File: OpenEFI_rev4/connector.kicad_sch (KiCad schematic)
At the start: 23 parts, among them J6 1241434-1, Q10 IRF540N, Q5 SS8050, Q6 IRLZ44N, Q7 IRLZ44N, U4 MIC2940A-3.3WU, U5 MIC2940A-5.0WT, U6 LT4363IMS

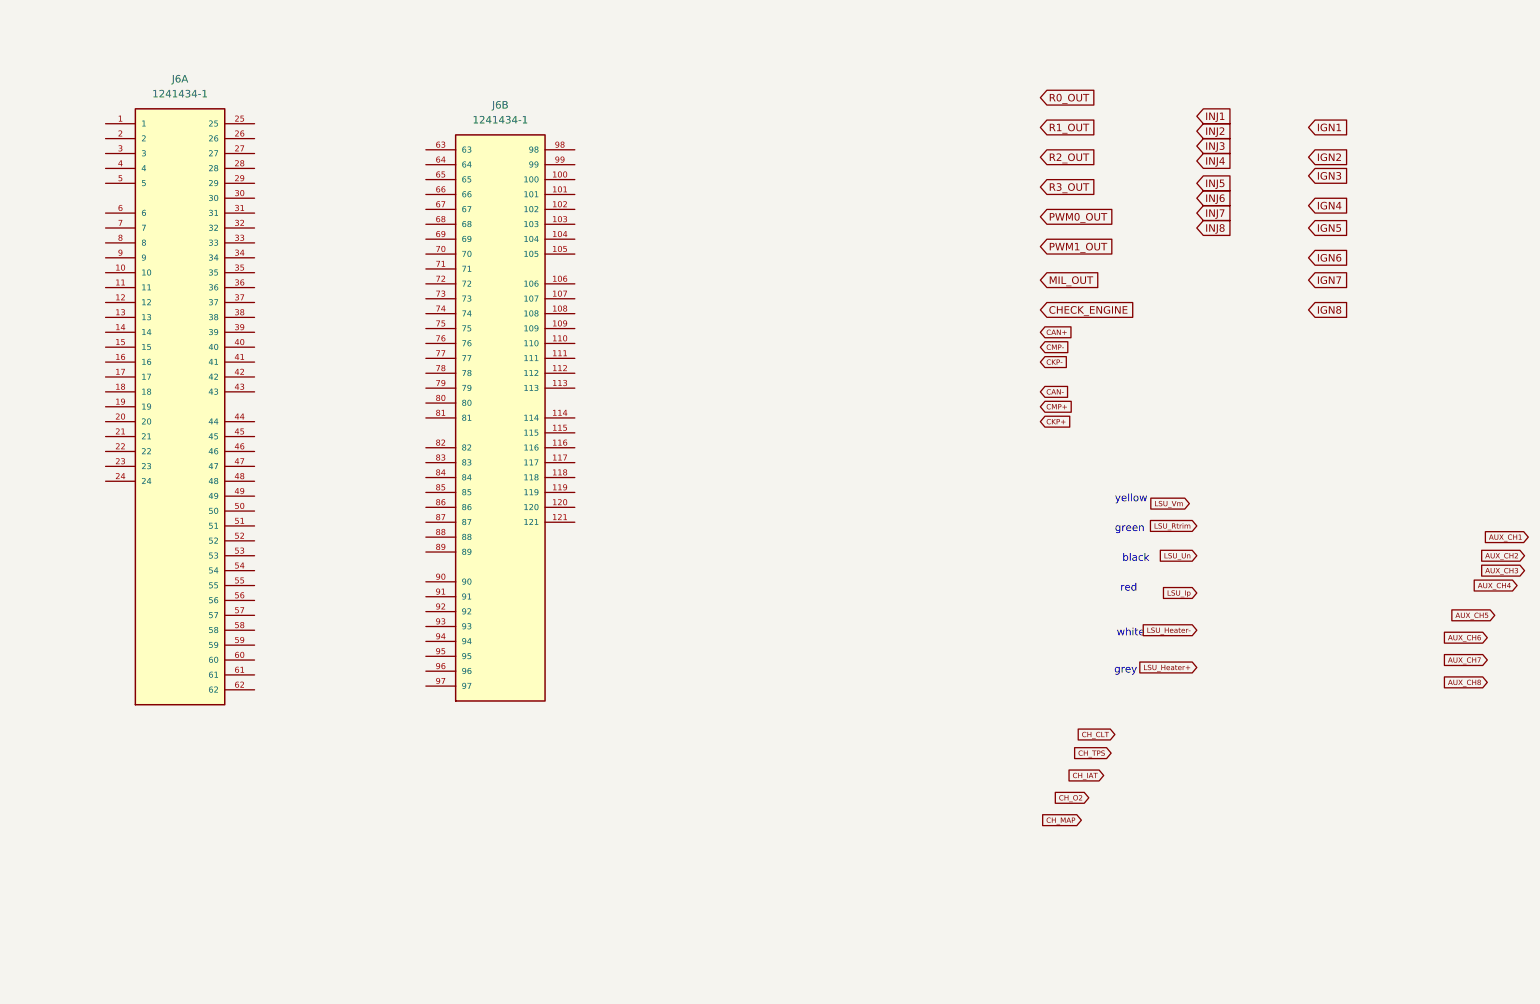
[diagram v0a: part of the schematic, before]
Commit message: update sensors/connector pinout, added rtc vbatt backup
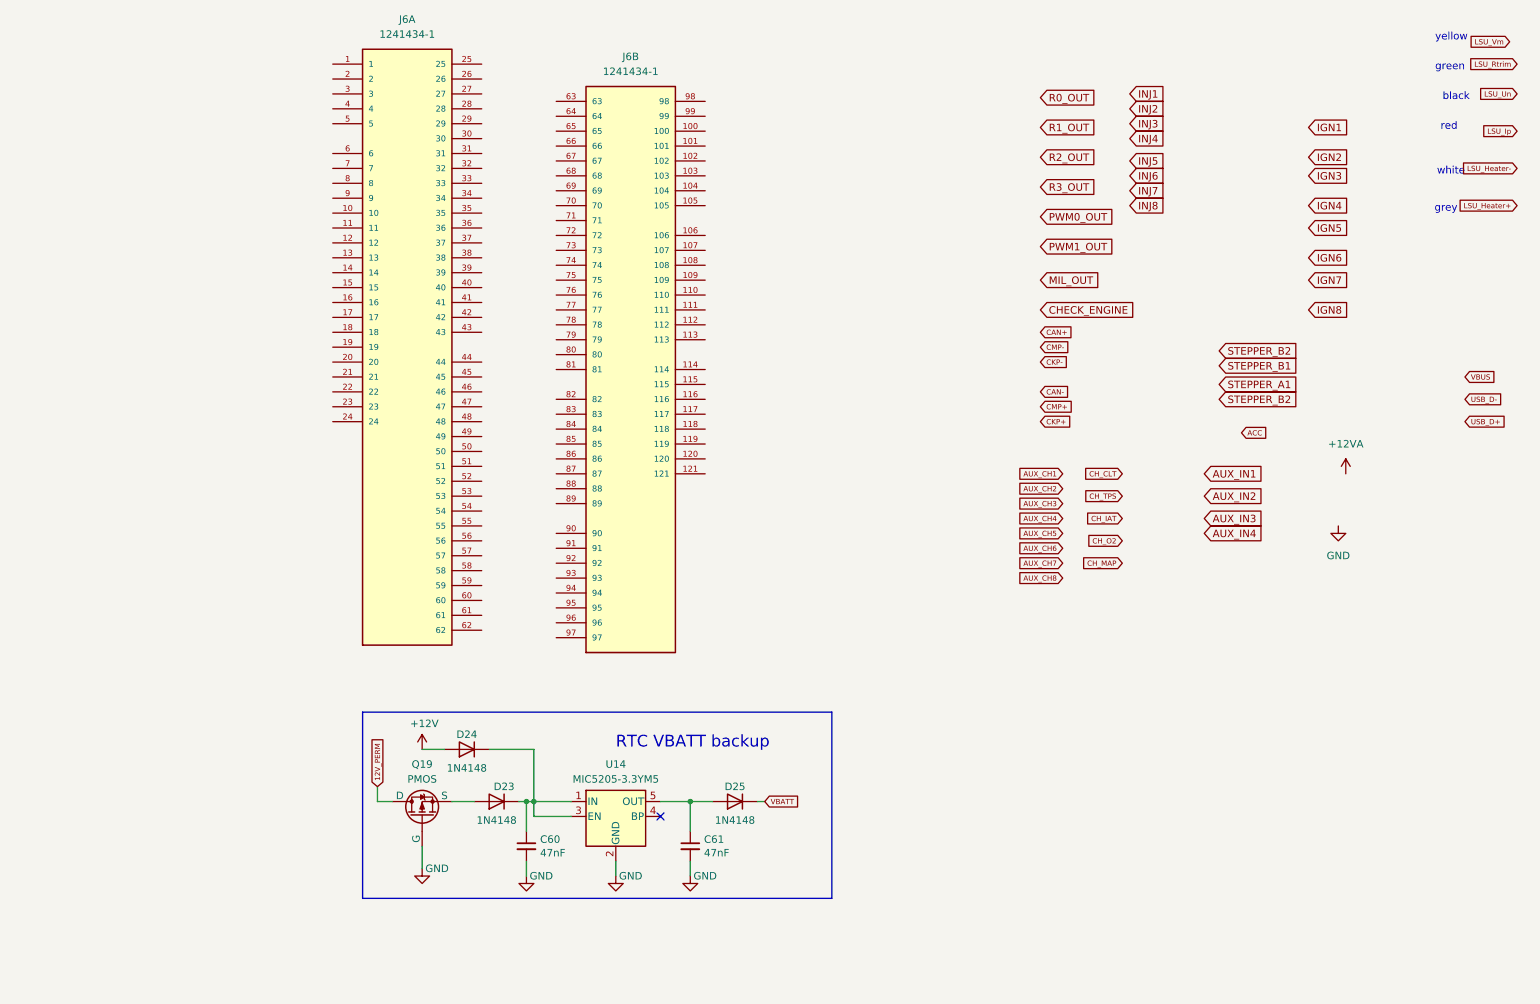
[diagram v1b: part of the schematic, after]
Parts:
- added C60, C61: 47nF, Capacitor_SMD:C_0603_1608Metric, symbol Device:C_Small
- added D23, D24, D25: 1N4148, Diode_SMD:D_SOD-523, symbol Diode:1N4148
- added Q19: PMOS, Package_TO_SOT_SMD:SOT-23-3, symbol Simulation_SPICE:PMOS
- added U14: MIC5205-3.3YM5, Package_TO_SOT_SMD:SOT-23-5, symbol Regulator_Linear:MIC5205-3.3YM5
- Q6, Q7: footprint Package_TO_SOT_THT:TO-220-3_Vertical -> Package_TO_SOT_SMD:TO-252-2; LCSC (none) -> C2584
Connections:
- net +12V: now also D24.2 (A)
- net GND: now also C60.2, C61.2, Q19.2 (G), U14.2 (GND)
- new net: C61.1, D25.2 (A), U14.5 (OUT)
- new net: C60.1, D23.1 (K), D24.1 (K), U14.1 (IN), U14.3 (EN)
- new net: D23.2 (A), Q19.3 (S)
- new net 12V_PERM: Q19.1 (D)
- new net VBATT: D25.1 (K)
- no-connect marks 5 -> 6
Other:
- note added: "RTC VBATT backup"
- moved on the sheet: J6A, J6B

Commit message: WIP Analog frontend
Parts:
- removed C31: 100uF ±20% 35V, Capacitor_SMD:CP_Elec_6.3x7.7, symbol Device:CP_Small
- removed Q19: PMOS, Package_TO_SOT_SMD:SOT-23-3, symbol Simulation_SPICE:PMOS
- removed U4: MIC2940A-3.3WU, Package_TO_SOT_SMD:TO-263-3_TabPin2, symbol Regulator_Linear:L7805
- removed U5: MIC2940A-5.0WT, Package_TO_SOT_THT:TO-220-3_Vertical, symbol Regulator_Linear:L7805
- added C42: 330uF ±20% 6.3V, Capacitor_SMD:CP_Elec_6.3x7.7, symbol Device:CP_Small
- added C62: 10nF, Capacitor_SMD:C_0805_2012Metric, symbol Device:C_Small
- added C64: 100nF, Capacitor_SMD:C_0805_2012Metric, symbol Device:C_Small
- added D26: B540C-13-F, Diode_SMD:D_SMA, symbol Device:D_Schottky
- added FL1: DLW21SZ900HQ2L, Library:FIL_DLW21SZ900HQ2L, symbol Library:DLW21SZ900HQ2L
- added L1: 10uH, Inductor_SMD:L_7.3x7.3_H4.5, symbol Device:L
- added Q20: PMN30XPX, Package_SO:TSOP-6_1.65x3.05mm_P0.95mm, symbol Transistor_FET:IRF540N
- added R2: 10k, Resistor_SMD:R_0603_1608Metric, symbol Device:R_Small
- added R2: 3.24k, Resistor_SMD:R_0603_1608Metric, symbol Device:R_Small
- added TP22, TP24, TP26, TP27, TP31, TP32, TP33, TP34, TP67, TP68, TP69, TP70, TP71, TP72, TP73, TP74: TestPoint, TestPoint:TestPoint_THTPad_1.5x1.5mm_Drill0.7mm, symbol Connector:TestPoint
- added U16: TPS5430DDA, Package_SO:TI_SO-PowerPAD-8_ThermalVias, symbol Regulator_Switching:TPS5430DDA
- added U17: L78M05ABDT-TR, Package_TO_SOT_SMD:TO-252-2, symbol Regulator_Linear:L7805
- Q10: value IRF540N -> PMN30XPX; footprint Package_TO_SOT_THT:TO-220-3_Vertical -> Package_SO:TSOP-6_1.65x3.05mm_P0.95mm; LCSC (none) -> C5288813
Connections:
- net +12V: now also Q10.4 (S), U16.7 (VIN)
- net +12VA: now also J6.3
- net +5V: now also C42.1, L1.2, R2.1; no longer Q10.3 (S)
- net +5VA: now also J6.25, J6.26, J6.27, J6.28, J6.29, J6.65, J6.78, J6.79, C64.1, U17.3 (OUT); no longer Q10.2 (D)
- net 12V_PERM: now also J6.62, Q20.4 (S)
- net ACC: now also J6.61
- net AUX_CH1: now also J6.70
- net AUX_CH2: now also J6.71
- net AUX_CH3: now also J6.72
- net AUX_CH4: now also J6.73
- net AUX_CH5: now also J6.74
- net AUX_CH6: now also J6.75
- net AUX_CH7: now also J6.76
- net AUX_CH8: now also J6.77
- net AUX_IN1: now also J6.30
- net AUX_IN2: now also J6.31
- net AUX_IN3: now also J6.32
- net AUX_IN4: now also J6.33
- net CAN+: now also J6.60
- net CAN-: now also J6.58
- net CHECK_ENGINE: now also J6.105
- net CH_CLT: now also J6.63
- net CH_IAT: now also J6.67
- net CH_MAP: now also J6.68
- net CH_O2: now also J6.69
- net CH_TPS: now also J6.64
- net CKP+: now also J6.10
- net CKP-: now also J6.11
- net CMP+: now also J6.12
- net CMP-: now also J6.13
- net GND: now also J6.1, J6.14, J6.15, J6.2, J6.50, J6.59, J6.66, J6.80, J6.81, C42.2, C64.2, D26.2 (A), Q20.3 (G), R2.2, U16.6 (GND), U16.9 (GNDPAD), U17.2 (GND)
- net IGN1: now also J6.106
- net IGN2: now also J6.107
- net IGN3: now also J6.108
- net IGN4: now also J6.109
- net IGN5: now also J6.110
- net IGN6: now also J6.111
- net IGN7: now also J6.112
- net IGN8: now also J6.113
- net INJ1: now also J6.114
- net INJ2: now also J6.115
- net INJ3: now also J6.116
- net INJ4: now also J6.117
- net INJ5: now also J6.118
- net INJ6: now also J6.119
- net INJ7: now also J6.120
- net INJ8: now also J6.121
- net LSU_Heater+: now also J6.4
- net LSU_Heater-: now also J6.5
- net LSU_Ip: now also J6.9
- net LSU_Rtrim: now also J6.7
- net LSU_Un: now also J6.8
- net LSU_Vm: now also J6.6
- net MIL_OUT: now also J6.104
- net PWM0_OUT: now also J6.102
- net PWM1_OUT: now also J6.103
- net R0_OUT: now also J6.98
- net R1_OUT: now also J6.99
- net R2_OUT: now also J6.100
- net R3_OUT: now also J6.101
- net STEPPER_A1: now also J6.20
- net STEPPER_B1: now also J6.22
- net STEPPER_B2: now also J6.23
- net USB_D+: now also FL1.1
- net USB_D-: now also FL1.4
- net VBUS: now also J6.47
- net at R33.2: now also Q10.3 (G); no longer Q10.1 (G)
- net at J6.82: now also TP34.1
- net at J6.83: now also TP33.1
- net at J6.84: now also TP32.1
- net at J6.85: now also TP31.1
- net at J6.86: now also TP27.1
- net at J6.87: now also TP26.1
- net at J6.88: now also TP24.1
- net at J6.89: now also TP22.1
- net at J6.90: now also TP74.1
- net at J6.91: now also TP73.1
- net at J6.92: now also TP72.1
- net at J6.93: now also TP71.1
- net at J6.94: now also TP70.1
- net at J6.95: now also TP69.1
- net at J6.96: now also TP68.1
- net at J6.97: now also TP67.1
- net at D23.2 (A): now also Q20.1 (D), Q20.2 (D), Q20.5 (D), Q20.6 (D)
- net STEPPER_A2: now reaches J6.21
- net USBD+: now reaches J6.48
- net USBD+: now also FL1.2
- net USBD-: now reaches J6.49
- net USBD-: now also FL1.3
- new net: C62.2, D26.1 (K), L1.1, U16.8 (PH)
- new net: C62.1, U16.1 (BOOT)
- new net: R2.1, R2.2, U16.4 (VSENSE)
- new net: Q10.1 (D), Q10.2 (D), Q10.5 (D), Q10.6 (D), U17.1 (IN)
- no-connect marks 6 -> 32
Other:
- note added: ">Para apantallado"
- note added: ">Para apantallado ckp/cmp"
- note added: "C1846"
- note added: "Para alimentar las entradas aux"
- note added: "Primer contacto"
- note added: "ign key"
- moved on the sheet: J6A, R33

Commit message: WIP analog frontend, init ckp"
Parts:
- added JP10, JP11, JP12: SolderJumper_2_Open, Jumper:SolderJumper-2_P1.3mm_Open_Pad1.0x1.5mm, symbol Jumper:SolderJumper_2_Open
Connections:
- net USB_D+: now also JP12.2 (B); no longer FL1.1
- net USB_D-: now also JP11.2 (B); no longer FL1.4
- net VBUS: now also JP10.2 (B); no longer J6.47
- new net: FL1.1, JP12.1 (A)
- new net: FL1.4, JP11.1 (A)
- new net VBUSC: J6.47, JP10.1 (A)
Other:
- moved on the sheet: FL1

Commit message: WIP relay driver
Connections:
- net CHECK_ENGINE: now also J6.104; no longer J6.105
- net MIL_OUT: now also J6.105; no longer J6.104
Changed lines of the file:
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@@
     )
   )
-  (global_label "MIL_OUT" (shape input) (at 267.97 43.18 0)
-    (effects (font (size 1.27 1.27)) (justify left))
-    (property "Intersheetrefs" "${INTERSHEET_REFS}" (at 272.8626 43.1006 0)
+  (global_label "MIL_OUT" (shape input) (at 261.62 45.72 0)
+    (effects (font (size 1.27 1.27)) (justify left))
+    (property "Intersheetrefs" "${INTERSHEET_REFS}" (at 266.5126 45.6406 0)
       (effects (font (size 1.27 1.27)) (justify left) hide)
     )
@@
     )
   )
-  (global_label "CHECK_ENGINE" (shape input) (at 261.62 45.72 0)
-    (effects (font (size 1.27 1.27)) (justify left))
-    (property "Intersheetrefs" "${INTERSHEET_REFS}" (at 266.3917 45.6406 0)
-      (effects (font (size 1.27 1.27)) (justify left) hide)
-    )
+  (global_label "CHECK_ENGINE" (shape input) (at 267.97 43.18 0)
+    (effects (font (size 1.27 1.27)) (justify left))
+    (property "Intersheetrefs" "${INTERSHEET_REFS}" (at 272.7417 43.1006 0)
+      (effects (font (size 1.27 1.27)) (justify left) hide)
+    )

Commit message: WIP CKP/CMP
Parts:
- added C65: 100nF, Capacitor_SMD:C_0805_2012Metric, symbol Device:C_Small
- added U4: AMS1117-3.3, Package_TO_SOT_SMD:SOT-223-3_TabPin2, symbol Regulator_Linear:AMS1117-3.3
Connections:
- net +5V: now also U4.3 (VI)
- net GND: now also C65.2, U4.1 (GND)
- new net +3V3: C65.1, U4.2 (VO)
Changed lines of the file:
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@@
   (junction (at 49.53 140.97) (diameter 1.016) (color 0 0 0 0)
   )
+  (junction (at 102.87 46.99) (diameter 0) (color 0 0 0 0)
+  )
   (junction (at 83.82 140.97) (diameter 1.016) (color 0 0 0 0)
   )
@@
     (stroke (width 0) (type solid))
   )
+  (wire (pts (xy 102.87 53.34) (xy 102.87 55.88))
+    (stroke (width 0) (type default))
+  )
   (wire (pts (xy 60.96 154.94) (xy 60.96 156.21))
     (stroke (width 0) (type solid))
@@
     (stroke (width 0) (type default))
   )
+  (wire (pts (xy 102.87 46.99) (xy 99.06 46.99))
+    (stroke (width 0) (type default))
+  )
   (wire (pts (xy 44.45 64.77) (xy 44.45 60.96))
     (stroke (width 0) (type solid))
@@
     (stroke (width 0) (type solid))
   )
+  (wire (pts (xy 80.01 46.99) (xy 83.82 46.99))
+    (stroke (width 0) (type default))
+  )
   (wire (pts (xy 68.58 46.99) (xy 68.58 49.53))
     (stroke (width 0) (type solid))
@@
     (stroke (width 0) (type default))
   )
+  (wire (pts (xy 102.87 44.45) (xy 102.87 46.99))
+    (stroke (width 0) (type default))
+  )
   (wire (pts (xy 141.478 45.72) (xy 147.32 45.72))
     (stroke (width 0) (type default))
@@
     (stroke (width 0) (type default))
   )
+  (wire (pts (xy 91.44 54.61) (xy 91.44 57.15))
+    (stroke (width 0) (type default))
+  )
+  (wire (pts (xy 80.01 45.72) (xy 80.01 46.99))
+    (stroke (width 0) (type default))
+  )
   (wire (pts (xy 83.82 151.13) (xy 64.77 151.13))
     (stroke (width 0) (type solid))
@@
     (stroke (width 0) (type solid))
   )
+  (wire (pts (xy 102.87 48.26) (xy 102.87 46.99))
+    (stroke (width 0) (type default))
+  )
   (wire (pts (xy 256.54 53.34) (xy 270.51 53.34))
     (stroke (width 0) (type default))
@@
     )
   )
+  (symbol (lib_id "Regulator_Linear:AMS1117-3.3") (at 91.44 46.99 0) (unit 1)
+    (in_bom yes) (on_board yes) (dnp no) (fields_autoplaced)
+    (property "Reference" "U4" (at 91.44 40.64 0)
+      (effects (font (size 1.27 1.27)))
+    )
+    (property "Value" "AMS1117-3.3" (at 91.44 43.18 0)
+      (effects (font (size 1.27 1.27)))
+    )
+    (property "Footprint" "Package_TO_SOT_SMD:SOT-223-3_TabPin2" (at 91.44 41.91 0)
+      (effects (font (size 1.27 1.27)) hide)
+    )
+    (property "Datasheet" "http://www.advanced-monolithic.com/pdf/ds1117.pdf" (at 93.98 53.34 0)
+      (effects (font (size 1.27 1.27)) hide)
+    )
+    (pin "1")
+    (pin "2")
+    (pin "3")
+    (instances
+      (project "OpenEFI_rev4"
+        (path "/b282ce4b-c3d0-4c94-b06c-73b92bb672a9/00000000-0000-0000-0000-00005f782f71"
+          (reference "U4") (unit 1)
+        )
+      )
+    )
+  )
   (symbol (lib_id "Connector:TestPoint") (at 223.52 114.3 90) (unit 1)
     (in_bom yes) (on_board yes) (dnp no) (fields_autoplaced)
@@
     )
   )
+  (symbol (lib_id "power:+3V3") (at 102.87 44.45 0) (unit 1)
+    (in_bom yes) (on_board yes) (dnp no)
+    (property "Reference" "#PWR0115" (at 102.87 48.26 0)
+      (effects (font (size 1.27 1.27)) hide)
+    )
+    (property "Value" "+3V3" (at 103.251 41.1988 90)
+      (effects (font (size 1.27 1.27)) (justify left))
+    )
+    (property "Footprint" "" (at 102.87 44.45 0)
+      (effects (font (size 1.27 1.27)) hide)
+    )
+    (property "Datasheet" "" (at 102.87 44.45 0)
+      (effects (font (size 1.27 1.27)) hide)
+    )
+    (pin "1")
+    (instances
+      (project "OpenEFI_rev4"
+        (path "/b282ce4b-c3d0-4c94-b06c-73b92bb672a9"
+          (reference "#PWR0115") (unit 1)
+        )
+        (path "/b282ce4b-c3d0-4c94-b06c-73b92bb672a9/00000000-0000-0000-0000-00005f782f71"
+          (reference "#PWR0203") (unit 1)
+        )
+      )
+    )
+  )
   (symbol (lib_id "Transistor_FET:IRLZ44N") (at 60.96 143.51 90) (unit 1)
     (in_bom yes) (on_board yes) (dnp no) (fields_autoplaced)
@@
     )
   )
+  (symbol (lib_id "Device:C_Small") (at 102.87 50.8 0) (unit 1)
+    (in_bom yes) (on_board yes) (dnp no)
+    (property "Reference" "C65" (at 104.14 48.895 0)
+      (effects (font (size 1.27 1.27)) (justify left))
+    )
+    (property "Value" "100nF" (at 102.87 52.07 0)
+      (effects (font (size 1.27 1.27)) (justify left) hide)
+    )
+    (property "Footprint" "Capacitor_SMD:C_0805_2012Metric" (at 102.87 50.8 0)
+      (effects (font (size 1.27 1.27)) hide)
+    )
+    (property "Datasheet" "~" (at 102.87 50.8 0)
+      (effects (font (size 1.27 1.27)) hide)
+    )
+    (property "LCSC" "C49678" (at 102.87 50.8 0)
+      (effects (font (size 1.27 1.27)) hide)
+    )
+    (pin "1")
+    (pin "2")
+    (instances
+      (project "OpenEFI_rev4"
+        (path "/b282ce4b-c3d0-4c94-b06c-73b92bb672a9/00000000-0000-0000-0000-00005f782f71"
+          (reference "C65") (unit 1)
+        )
+      )
+    )
+  )
   (symbol (lib_id "power:+12V") (at 22.86 83.82 0) (unit 1)
     (in_bom yes) (on_board yes) (dnp no)
@@
     )
   )
+  (symbol (lib_id "power:+5V") (at 80.01 45.72 0) (unit 1)
+    (in_bom yes) (on_board yes) (dnp no) (fields_autoplaced)
+    (property "Reference" "#PWR0199" (at 80.01 49.53 0)
+      (effects (font (size 1.27 1.27)) hide)
+    )
+    (property "Value" "+5V" (at 80.01 40.64 0)
+      (effects (font (size 1.27 1.27)))
+    )
+    (property "Footprint" "" (at 80.01 45.72 0)
+      (effects (font (size 1.27 1.27)) hide)
+    )
+    (property "Datasheet" "" (at 80.01 45.72 0)
+      (effects (font (size 1.27 1.27)) hide)
+    )
+    (pin "1")
+    (instances
+      (project "OpenEFI_rev4"
+        (path "/b282ce4b-c3d0-4c94-b06c-73b92bb672a9/00000000-0000-0000-0000-00005f782f71"
+          (reference "#PWR0199") (unit 1)
+        )
+      )
+    )
+  )
   (symbol (lib_id "power:GND") (at 81.28 104.14 0) (unit 1)
     (in_bom yes) (on_board yes) (dnp no)
@@
     )
   )
+  (symbol (lib_id "power:GND") (at 91.44 57.15 0) (unit 1)
+    (in_bom yes) (on_board yes) (dnp no)
+    (property "Reference" "#PWR0164" (at 91.44 63.5 0)
+      (effects (font (size 1.27 1.27)) hide)
+    )
+    (property "Value" "GND" (at 91.567 61.5442 0)
+      (effects (font (size 1.27 1.27)))
+    )
+    (property "Footprint" "" (at 91.44 57.15 0)
+      (effects (font (size 1.27 1.27)) hide)
+    )
+    (property "Datasheet" "" (at 91.44 57.15 0)
+      (effects (font (size 1.27 1.27)) hide)
+    )
+    (pin "1")
+    (instances
+      (project "OpenEFI_rev4"
+        (path "/b282ce4b-c3d0-4c94-b06c-73b92bb672a9/00000000-0000-0000-0000-00005f782f71"
+          (reference "#PWR0164") (unit 1)
+        )
+      )
+    )
+  )
   (symbol (lib_id "Device:CP_Small") (at 87.63 90.17 0) (unit 1)
     (in_bom yes) (on_board yes) (dnp no)
@@
         )
       )
+    )
+  )
+  (symbol (lib_id "power:GND") (at 102.87 55.88 0) (unit 1)
+    (in_bom yes) (on_board yes) (dnp no)
+    (property "Reference" "#PWR0131" (at 102.87 62.23 0)
+      (effects (font (size 1.27 1.27)) hide)
+    )
+    (property "Value" "GND" (at 102.997 60.2742 0)
+      (effects (font (size 1.27 1.27)))
+    )
+    (property "Footprint" "" (at 102.87 55.88 0)
+      (effects (font (size 1.27 1.27)) hide)
+    )
+    (property "Datasheet" "" (at 102.87 55.88 0)
+      (effects (font (size 1.27 1.27)) hide)
+    )
+    (pin "1")
+    (instances
+      (project "OpenEFI_rev4"
+        (path "/b282ce4b-c3d0-4c94-b06c-73b92bb672a9/00000000-0000-0000-0000-00005f782f71"
+          (reference "#PWR0131") (unit 1)
+        )
+      )
